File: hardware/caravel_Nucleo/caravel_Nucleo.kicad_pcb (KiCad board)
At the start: 2 copper layers, 68.1 x 92.5 mm, 91 parts, among them J1 USB_B_Micro - 10118193-0001LF, J10 Conn_01x11_Female, J11 Conn_01x02, J12 Conn_01x02_Male, J2 Conn_01x02_Female, J3 Conn_01x02_Male, J4 Conn_01x04_Female, J5 Conn_01x02_Male, J6 Conn_01x02_Male, J7 Conn_01x06_Female, J8 Conn_01x03, J9 Conn_01x03, SW1 SW_Push - SKQGADE010, T1 Logo, T2 Logo, U1 FT232H, U10 MCP4661, U11 TAR5SxxU_SOT353F, U12 NUCLEO144-F746ZG, U2 SN74LVC1G125DCKR, U3 SN74LVC1G125DCKR, U4 MCP1319MT-29LE-OT, U5 TAR5SxxU_SOT353F, U6 TAR5SxxU_SOT353F, U7 W25Q32FVSS, U8 caravel_breakout, U9 MIC2211-AAYML-TR, X1 DSC6001_10MHZ, Y1 CSTNE12M0GH5L000R0

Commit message: Move components to local library
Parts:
- C1, C10, C11, C12, C13, C14, C15, C16, C17, C18, C19, C2, C20, C21, C22, C23, C24, C3, C4, C5, C6, C7, C8, C9: footprint Capacitor_SMD:C_0805_2012Metric -> caravel_Nucleo-footprints:C_0805_2012Metric
- D1, D2, D3, D4: footprint LED_SMD:LED_1206_3216Metric -> caravel_Nucleo-footprints:LED_1206_3216Metric
- J1: footprint strive_foot_prints:FCI_10118193-0001LF -> caravel_Nucleo-footprints:FCI_10118193-0001LF
- J10: footprint Connector_PinHeader_2.54mm:PinHeader_1x11_P2.54mm_Vertical -> caravel_Nucleo-footprints:PinHeader_1x11_P2.54mm_Vertical
- J11, J12, J2, J3, J5, J6: footprint Connector_PinHeader_2.54mm:PinHeader_1x02_P2.54mm_Vertical -> caravel_Nucleo-footprints:PinHeader_1x02_P2.54mm_Vertical
- J4: footprint Connector_PinHeader_2.54mm:PinHeader_1x04_P2.54mm_Vertical -> caravel_Nucleo-footprints:PinHeader_1x04_P2.54mm_Vertical
- J7: footprint Connector_PinHeader_2.54mm:PinHeader_1x06_P2.54mm_Vertical -> caravel_Nucleo-footprints:PinHeader_1x06_P2.54mm_Vertical
- J8, J9: footprint Connector_PinHeader_2.54mm:PinHeader_1x03_P2.54mm_Vertical -> caravel_Nucleo-footprints:PinHeader_1x03_P2.54mm_Vertical
- R1, R10, R11, R12, R13, R14, R15, R16, R17, R18, R19, R2, R20, R21, R22, R23, R24, R25, R26, R27, R28, R29, R3, R30, R31, R32, R33, R4, R5, R6, R7, R8, R9: footprint Resistor_SMD:R_0805_2012Metric -> caravel_Nucleo-footprints:R_0805_2012Metric
- SW1: footprint strive_foot_prints:SW4-SMD-5.2X5.2X1.5MM -> caravel_Nucleo-footprints:SW4-SMD-5.2X5.2X1.5MM
- T1: footprint Caravel_Board:logo -> caravel_Nucleo-footprints:logo
- T2: footprint Caravel_Board:ef_logo -> caravel_Nucleo-footprints:ef_logo
- TP1: footprint TestPoint:TestPoint_Bridge_Pitch2.54mm_Drill1.0mm -> caravel_Nucleo-footprints:TestPoint_Bridge_Pitch2.54mm_Drill1.0mm
- U1: footprint Package_DFN_QFN:QFN-48-1EP_8x8mm_P0.5mm_EP6.2x6.2mm -> caravel_Nucleo-footprints:QFN-48-1EP_8x8mm_P0.5mm_EP6.2x6.2mm
- U10: footprint Caravel_Board:QFN-16-1EP_4x4mm_P0.65mm_EP2.5x2.5mm -> caravel_Nucleo-footprints:QFN-16-1EP_4x4mm_P0.65mm_EP2.5x2.5mm
- U11, U5, U6: footprint Caravel_Board:SOT-353F -> caravel_Nucleo-footprints:SOT-353F
- U12: footprint Caravel_Board:ST_Morpho_Connectors_144 -> caravel_Nucleo-footprints:ST_Morpho_Connectors_144
- U2, U3: footprint strive_foot_prints:SOT65P210X110-5N -> caravel_Nucleo-footprints:SOT65P210X110-5N
- U4: footprint Caravel_Board:PoR_5_SOT23 -> caravel_Nucleo-footprints:PoR_5_SOT23
- U7: footprint strive_foot_prints:SOIC127P790X216-8N -> caravel_Nucleo-footprints:SOIC127P790X216-8N
- U8: footprint Caravel_Board:caravel_breakout_flexy_rev3D -> caravel_Nucleo-footprints:caravel_breakout_flexy_rev3D
- U9: footprint Caravel_Board:10-pin_MLF_P0.5 -> caravel_Nucleo-footprints:10-pin_MLF_P0.5
- X1: footprint strive_foot_prints:DSC6001JE1A-010.0000 -> caravel_Nucleo-footprints:DSC6001JE1A-010.0000
- Y1: footprint strive_foot_prints:CSTNE12M0GH5L000R0 -> caravel_Nucleo-footprints:CSTNE12M0GH5L000R0

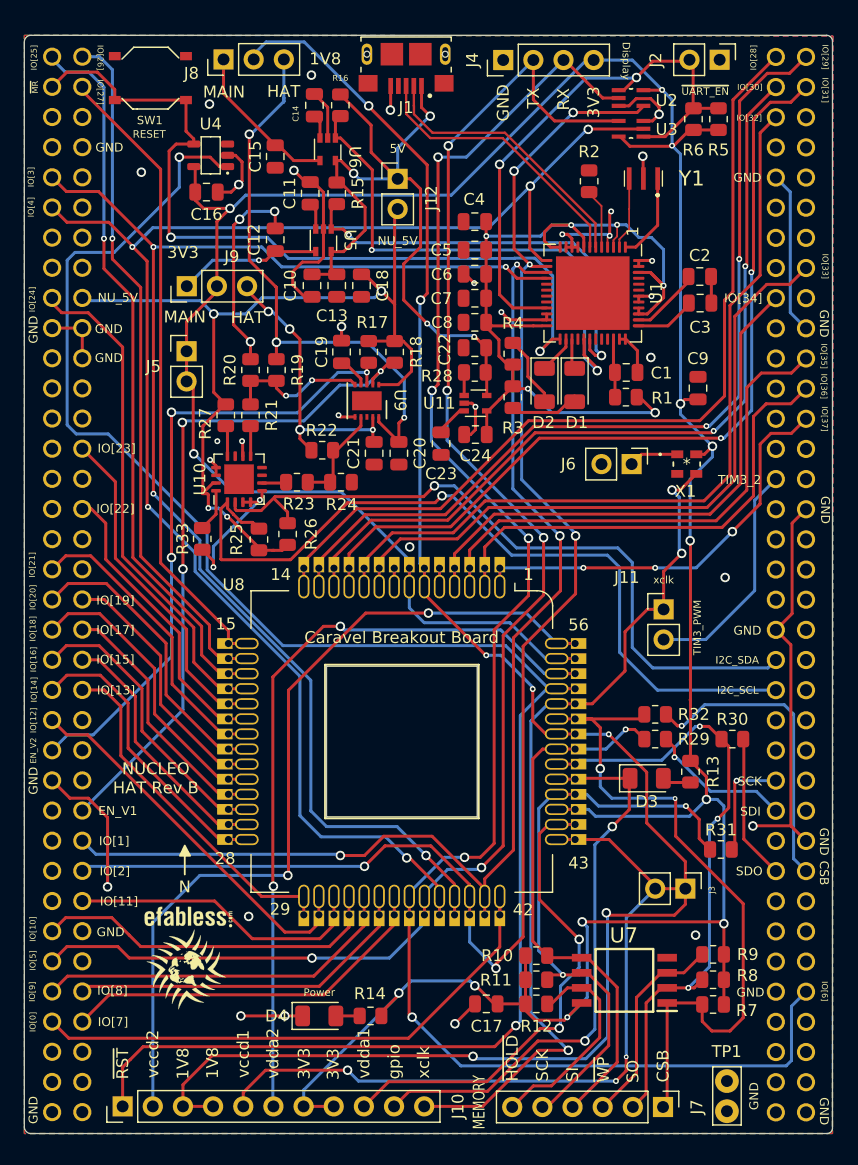
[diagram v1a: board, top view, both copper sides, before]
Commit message: Update PCB components
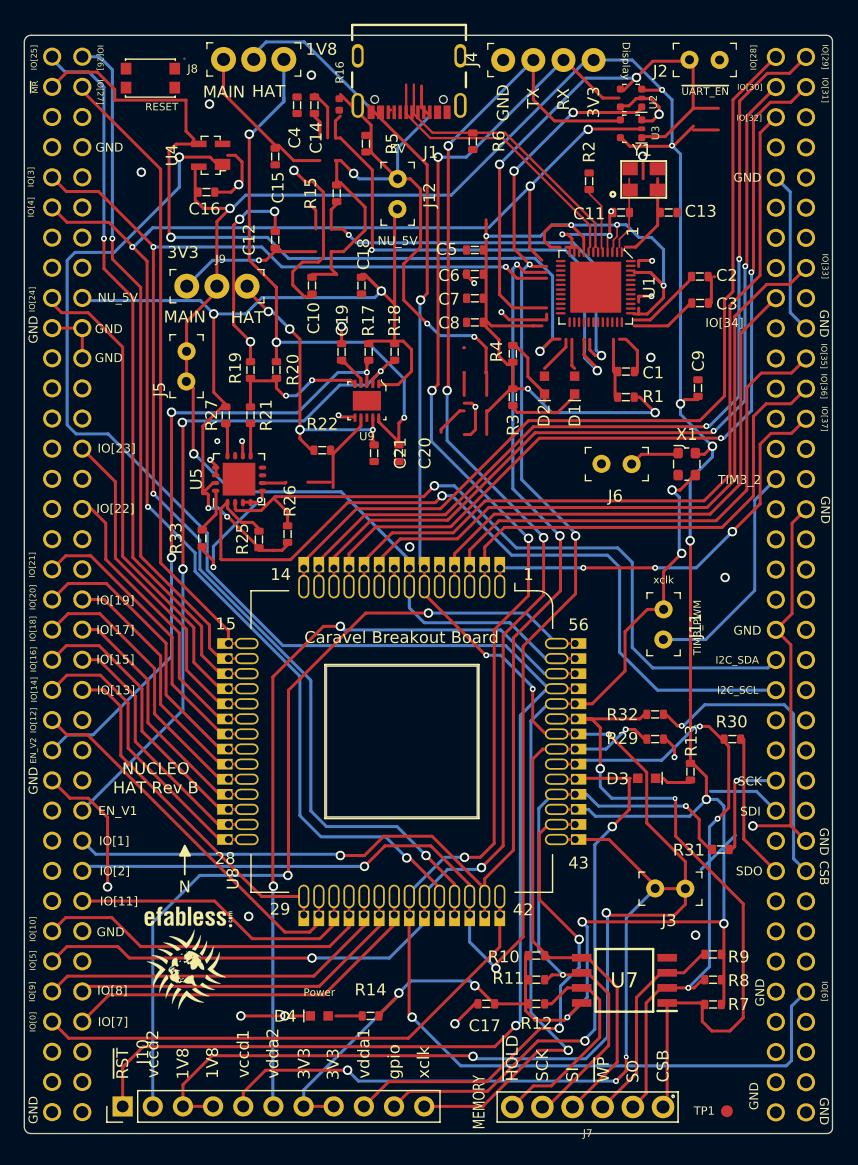
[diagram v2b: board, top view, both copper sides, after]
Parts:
- removed C22: 1uf - CC0805KKX5R8BB105, caravel_Nucleo-footprints:C_0805_2012Metric
- removed C23: 0.01uf - CC0805KRX7R9BB103, caravel_Nucleo-footprints:C_0805_2012Metric
- removed C24: 10uf - CC0805KKX5R8BB106, caravel_Nucleo-footprints:C_0805_2012Metric
- removed R23: 4.99K 1% - 0805W8F1202T5E, caravel_Nucleo-footprints:R_0805_2012Metric
- removed R24: 4.02K 1% - 0805W8F1202T5E, caravel_Nucleo-footprints:R_0805_2012Metric
- removed R28: 10k, caravel_Nucleo-footprints:R_0805_2012Metric
- removed U10: MCP4661, caravel_Nucleo-footprints:QFN-16-1EP_4x4mm_P0.65mm_EP2.5x2.5mm
- removed U11, U6: TAR5SxxU_SOT353F, caravel_Nucleo-footprints:SOT-353F
- C1: value 0.01uf - CC0805JRX7R9BB103 -> C_10n_0603; footprint caravel_Nucleo-footprints:C_0805_2012Metric -> antmicro-footprints:0603-cap
- C10: value 1uf - CC0805KKX5R8BB105 -> C_4u7_0603; footprint caravel_Nucleo-footprints:C_0805_2012Metric -> antmicro-footprints:0603-cap
- C11: value 0.01uf - CC0805KRX7R9BB103 -> C_18p_0603; footprint caravel_Nucleo-footprints:C_0805_2012Metric -> antmicro-footprints:0603-cap
- C12, C15: value 10uf - CC0805KKX5R8BB106 -> C_100n_0603; footprint caravel_Nucleo-footprints:C_0805_2012Metric -> antmicro-footprints:0603-cap
- C13: value 1uf - CC0805KKX5R8BB105 -> C_18p_0603; footprint caravel_Nucleo-footprints:C_0805_2012Metric -> antmicro-footprints:0603-cap
- C14: value 0.01uf - CC0805KRX7R9BB103 -> C_4u7_0603; footprint caravel_Nucleo-footprints:C_0805_2012Metric -> antmicro-footprints:0603-cap
- C16, C17, C2, C3, C4, C5, C6, C7, C8, C9: value 0.1uf - CC0805KRX7R9BB104 -> C_100n_0603; footprint caravel_Nucleo-footprints:C_0805_2012Metric -> antmicro-footprints:0603-cap
- C18, C20, C21: value 1uf - CC0805KKX5R8BB105 -> C_1u_0603; footprint caravel_Nucleo-footprints:C_0805_2012Metric -> antmicro-footprints:0603-cap
- C19: value 0.01uf - CC0805KRX7R9BB103 -> C_10n_0603; footprint caravel_Nucleo-footprints:C_0805_2012Metric -> antmicro-footprints:0603-cap
- D1, D2, D3, D4: value LED - 17-215SURC/S530-A2/TR8 -> KP-1608ZGC; footprint caravel_Nucleo-footprints:LED_1206_3216Metric -> antmicro-footprints:LED_0603
- J1: value USB_B_Micro - 10118193-0001LF -> USB4105-GF-A; footprint caravel_Nucleo-footprints:FCI_10118193-0001LF -> antmicro-footprints:GCT_USB4105-GF-A
- J10: value Conn_01x11_Female -> PinHeader_1x11; footprint caravel_Nucleo-footprints:PinHeader_1x11_P2.54mm_Vertical -> antmicro-footprints:PinHeader_1x11_P2.54_Vertical
- J11: value Conn_01x02 -> PinHeader_1x02; footprint caravel_Nucleo-footprints:PinHeader_1x02_P2.54mm_Vertical -> antmicro-footprints:PinHeader_1x2_P2.54mm
- J12, J3, J5, J6: value Conn_01x02_Male -> PinHeader_1x02; footprint caravel_Nucleo-footprints:PinHeader_1x02_P2.54mm_Vertical -> antmicro-footprints:PinHeader_1x2_P2.54mm
- J2: value Conn_01x02_Female -> M20-9990246; footprint caravel_Nucleo-footprints:PinHeader_1x02_P2.54mm_Vertical -> antmicro-footprints:PinHeader_1x2_P2.54mm
- J4: value Conn_01x04_Female -> 61300411121; footprint caravel_Nucleo-footprints:PinHeader_1x04_P2.54mm_Vertical -> antmicro-footprints:PinHeader_1x4_P2.54mm_Drill1.02mm
- J7: value Conn_01x06_Female -> 61300611121; footprint caravel_Nucleo-footprints:PinHeader_1x06_P2.54mm_Vertical -> antmicro-footprints:61300611121
- J8, J9: value Conn_01x03 -> 640456-3; footprint caravel_Nucleo-footprints:PinHeader_1x03_P2.54mm_Vertical -> antmicro-footprints:PinHeader_1x3_P2.54_Drill1.1mm
- R1, R10, R11, R12, R7, R8, R9: value 10k - RC0805FR-0710KL -> R_10k_0603; footprint caravel_Nucleo-footprints:R_0805_2012Metric -> antmicro-footprints:0603-res
- R13, R14: value 82 - 0805W8F820JT5E -> R_470R_0603; footprint caravel_Nucleo-footprints:R_0805_2012Metric -> antmicro-footprints:0603-res
- R15: value 10k -> R_15k_0603; footprint caravel_Nucleo-footprints:R_0805_2012Metric -> antmicro-footprints:0603-res
- R16: value 10k -> R_34k_0402; footprint caravel_Nucleo-footprints:R_0805_2012Metric -> antmicro-footprints:0402-res
- R17, R18, R27: value 10k -> R_10k_0603; footprint caravel_Nucleo-footprints:R_0805_2012Metric -> antmicro-footprints:0603-res
- R19: value 360 1% - 0805W8F1202T5E -> R_68k_0603; footprint caravel_Nucleo-footprints:R_0805_2012Metric -> antmicro-footprints:0603-res
- R2: value 12K 1% - 0805W8F1202T5E -> R_12k_0603; footprint caravel_Nucleo-footprints:R_0805_2012Metric -> antmicro-footprints:0603-res
- R20: value 4.99K 1% - 0805W8F1202T5E -> R_41k2_0603; footprint caravel_Nucleo-footprints:R_0805_2012Metric -> antmicro-footprints:0603-res
- R21: value 499 1% - 0805W8F1202T5E -> R_10k_0603; footprint caravel_Nucleo-footprints:R_0805_2012Metric -> antmicro-footprints:0603-res
- R22: value 4.22K 1% - 0805W8F1202T5E -> R_10k_0603; footprint caravel_Nucleo-footprints:R_0805_2012Metric -> antmicro-footprints:0603-res
- R25, R26: value 4.7K 1% - 0805W8F1202T5E -> R_4k7_0603; footprint caravel_Nucleo-footprints:R_0805_2012Metric -> antmicro-footprints:0603-res
- R29, R30, R31, R32, R33: value 0 -> R_0R_0603; footprint caravel_Nucleo-footprints:R_0805_2012Metric -> antmicro-footprints:0603-res
- R3, R4: value 150 - 0805W8J0151T5E -> R_470R_0603; footprint caravel_Nucleo-footprints:R_0805_2012Metric -> antmicro-footprints:0603-res
- R5, R6: value 10k -> R_5k1_0603; footprint caravel_Nucleo-footprints:R_0805_2012Metric -> antmicro-footprints:0603-res
- SW1: value SW_Push - SKQGADE010 -> KMR2; footprint caravel_Nucleo-footprints:SW4-SMD-5.2X5.2X1.5MM -> antmicro-footprints:SW_SPST_4.2x2.8
- T1: footprint caravel_Nucleo-footprints:logo -> antmicro-footprints:efabless_logo_2
- T2: footprint caravel_Nucleo-footprints:ef_logo -> antmicro-footprints:efabless_logo
- TP1: value TestPoint -> TP_SMD1MM; footprint caravel_Nucleo-footprints:TestPoint_Bridge_Pitch2.54mm_Drill1.0mm -> antmicro-footprints:Testpoint_smd_1mm
- U1: value FT232H -> FT232HQ; footprint caravel_Nucleo-footprints:QFN-48-1EP_8x8mm_P0.5mm_EP6.2x6.2mm -> antmicro-footprints:QFN-48-1EP_6x6mm
- U12: value NUCLEO144-F746ZG -> NUCLEO144-F429ZI; footprint caravel_Nucleo-footprints:ST_Morpho_Connectors_144 -> antmicro-footprints:ST_Morpho_Connectors_144
- U2, U3: footprint caravel_Nucleo-footprints:SOT65P210X110-5N -> antmicro-footprints:SOT-353
- U4: value MCP1319MT-29LE-OT -> MAX811REUS+T; footprint caravel_Nucleo-footprints:PoR_5_SOT23 -> antmicro-footprints:SOT-143-4
- U5: value TAR5SxxU_SOT353F -> MCP4661-103E/ML; footprint caravel_Nucleo-footprints:SOT-353F -> antmicro-footprints:QFN-16_EP_4x4_Pitch0.65mm
- U7: footprint caravel_Nucleo-footprints:SOIC127P790X216-8N -> antmicro-footprints:SOIC127P790X216-8N
- U8: footprint caravel_Nucleo-footprints:caravel_breakout_flexy_rev3D -> antmicro-footprints:caravel_breakout
- U9: footprint caravel_Nucleo-footprints:10-pin_MLF_P0.5 -> antmicro-footprints:DFN-10-1EP_3x3mm
- X1: value DSC6001_10MHZ -> ECS-2520MVLC-100-BN-TR; footprint caravel_Nucleo-footprints:DSC6001JE1A-010.0000 -> antmicro-footprints:Oscillator_SMD_ECS_2520MV-xxx-xx-4Pin_2.5x2.0mm
- Y1: value CSTNE12M0GH5L000R0 -> ABM8G-12.000MHZ-18-D2Y-T; footprint caravel_Nucleo-footprints:CSTNE12M0GH5L000R0 -> antmicro-footprints:KX-7
- moved R5 29.8 mm to (128.8, 26.5), turned to -90 degrees
- moved C13 28.6 mm to (154.3, 32.3), turned to 0 degrees
- moved C11 26.2 mm to (150.3, 32.3), turned to 180 degrees
- moved U5 21.3 mm to (118.1, 54.8), turned to 90 degrees
- moved R6 18.7 mm to (137.8, 26.3), turned to -90 degrees
- moved C4 17.9 mm to (123.0, 23.3), turned to 90 degrees
- moved J7 6.35 mm to (147.5, 107.6), turned to 180 degrees
- moved TP1 2.54 mm to (159.2, 108.0), turned to 0 degrees
- moved U1 0.56 mm to (148.2, 38.6)
- moved J1 0.28 mm to (132.4, 19.1)
- moved R16 0.12 mm to (126.5, 23.2), turned to -90 degrees
- moved C1 0.07 mm to (150.7, 45.7), turned to 0 degrees
- turned J2 to 180 degrees
- turned J12 to -90 degrees
- turned J3 to 180 degrees
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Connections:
- net EN_VOUT1 renamed /EN_VOUT1
- net EN_VOUT2 renamed /EN_VOUT2
- net Net-(C2-Pad2) renamed /VCORE
- net Net-(C3-Pad2) renamed /VCCA
- net Net-(R2-Pad2) renamed /REF
- net SPI5_CS renamed /SPI5_CS
- net SPI5_MISO renamed /SPI5_MISO
- net SPI5_MOSI renamed /SPI5_MOSI
- net SPI5_SCK renamed /SPI5_SCK
- net TIM3_CH2 renamed /TIM3_CH2
- net UART8_RX renamed /UART8_RX
- net UART8_TX renamed /UART8_TX
- net mprj_io[0] renamed /mprj_io[0]
- net mprj_io[10] renamed /mprj_io[10]
- net mprj_io[11] renamed /mprj_io[11]
- net mprj_io[12] renamed /mprj_io[12]
- net mprj_io[13] renamed /mprj_io[13]
- net mprj_io[14] renamed /mprj_io[14]
- net mprj_io[15] renamed /mprj_io[15]
- net mprj_io[16] renamed /mprj_io[16]
- net mprj_io[17] renamed /mprj_io[17]
- net mprj_io[18] renamed /mprj_io[18]
- net mprj_io[19] renamed /mprj_io[19]
- net mprj_io[20] renamed /mprj_io[20]
- net mprj_io[21] renamed /mprj_io[21]
- net mprj_io[22] renamed /mprj_io[22]
- net mprj_io[23] renamed /mprj_io[23]
- net mprj_io[24] renamed /mprj_io[24]
- net mprj_io[25] renamed /mprj_io[25]
- net mprj_io[26] renamed /mprj_io[26]
- net mprj_io[27] renamed /mprj_io[27]
- net mprj_io[28] renamed /mprj_io[28]
- net mprj_io[29] renamed /mprj_io[29]
- net mprj_io[30] renamed /mprj_io[30]
- net mprj_io[31] renamed /mprj_io[31]
- net mprj_io[32] renamed /mprj_io[32]
- net mprj_io[33] renamed /mprj_io[33]
- net mprj_io[34] renamed /mprj_io[34]
- net mprj_io[35] renamed /mprj_io[35]
- net mprj_io[36] renamed /mprj_io[36]
- net mprj_io[37] renamed /mprj_io[37]
- net mprj_io[7] renamed /mprj_io[7]
- net mprj_io[8] renamed /mprj_io[8]
- net mprj_io[9] renamed /mprj_io[9]
- net vccd2 renamed /vccd2
- net vdda1 renamed /vdda1
- net vdda2 renamed /vdda2
- C1 pad 1: GND -> /FTDI_RESET
- C1 pad 2: Net-(C1-Pad2) -> AGND
- C10 pad 1: GND -> VBUS
- C10 pad 2: +5V -> AGND
- C11 pad 1: Net-(C11-Pad1) -> /XIN
- C11 pad 2: GND -> AGND
- C12 pad 1: GND -> AGND
- C12 pad 2: V3.3 -> VBUS
- C13 pad 1: GND -> /XOUT
- C13 pad 2: +5V -> AGND
- C14 pad 1: Net-(C14-Pad1) -> /FTDI_3V3
- C14 pad 2: GND -> AGND
- C15 pad 1: GND -> AGND
- C15 pad 2: V1.8 -> /FTDI_3V3
- C16 pad 1: GND -> +3V3
- C16 pad 2: vdda -> AGND
- C17 pad 1: vdda -> +3V3
- C17 pad 2: GND -> AGND
- C18 pad 1: GND -> /NU_5V
- C18 pad 2: NU_5V -> AGND
- C19 pad 1: Net-(C19-Pad1) -> AGND
- C19 pad 2: GND -> Net-(C19-Pad2)
- C2 pad 1: GND -> AGND
- C20 pad 1: VOUT1 -> +3V3
- C20 pad 2: GND -> AGND
- C21 pad 1: VOUT2 -> +1V8
- C21 pad 2: GND -> AGND
- C3 pad 1: GND -> AGND
- C4 pad 1: GND -> /FTDI_3V3
- C4 pad 2: FTDI_V3.3 -> AGND
- C5 pad 1: GND -> /FTDI_3V3
- C5 pad 2: FTDI_V3.3 -> AGND
- C6 pad 1: GND -> /FTDI_3V3
- C6 pad 2: FTDI_V3.3 -> AGND
- C7 pad 1: GND -> /FTDI_3V3
- C7 pad 2: FTDI_V3.3 -> AGND
- C8 pad 1: GND -> /FTDI_3V3
- C8 pad 2: FTDI_V3.3 -> AGND
- C9 pad 1: GND -> AGND
- C9 pad 2: vdda -> +3V3
- D1 pad 1: Net-(D1-Pad1) -> /FTDI_3V3
- D2 pad 1: Net-(D2-Pad1) -> /FTDI_3V3
- D3 pad 1: gpio -> Net-(D3-Pad1)
- D3 pad 2: Net-(D3-Pad2) -> /gpio
- D4 pad 1: GND -> Net-(D4-Pad1)
- D4 pad 2: Net-(D4-Pad2) -> AGND
- J10 pad 10: gpio -> /gpio
- J10 pad 3: vccd -> +1V8
- J10 pad 4: vccd -> +1V8
- J10 pad 5: vccd -> +1V8
- J10 pad 7: vdda -> +3V3
- J10 pad 8: vdda -> +3V3
- J12 pad 2: NU_5V -> /NU_5V
- J2 pad 1: GND -> AGND
- J2 pad 2: ~{UART_EN} -> /~{UART_EN}
- J3 pad 1: vccd -> +1V8
- J3 pad 2: vccd -> +1V8
- J4 pad 1: GND -> AGND
- J4 pad 4: vdda -> +3V3
- J5 pad 1: vdda -> +3V3
- J5 pad 2: vdda -> +3V3
- J6 pad 2: GND -> AGND
- J7 pad 1: Caravel_CSB -> /Caravel_CSB
- J7 pad 2: Caravel_D1 -> /Caravel_D1
- J7 pad 3: ~{MEM_WP} -> /~{MEM_WP}
- J7 pad 4: Caravel_D0 -> /Caravel_D0
- J7 pad 5: Caravel_SCK -> /Caravel_SCK
- J7 pad 6: ~{MEM_HOLD} -> /~{MEM_HOLD}
- J8 pad 1: V1.8 -> /P0B
- J8 pad 2: vccd -> /P0A
- J8 pad 3: VOUT1 -> unconnected-(J8-Pad3)
- J9 pad 1: V3.3 -> /P1B
- J9 pad 2: vdda -> /P1A
- J9 pad 3: VOUT2 -> /LV_BOOSTER
- R1 pad 1: Net-(C1-Pad2) -> /FTDI_3V3
- R1 pad 2: FTDI_V3.3 -> /FTDI_RESET
- R10 pad 1: Caravel_D0 -> +3V3
- R10 pad 2: vdda -> /Caravel_D0
- R11 pad 1: Caravel_SCK -> +3V3
- R11 pad 2: vdda -> /Caravel_SCK
- R12 pad 1: ~{MEM_HOLD} -> +3V3
- R12 pad 2: vdda -> /~{MEM_HOLD}
- R13 pad 1: vdda -> Net-(D3-Pad1)
- R13 pad 2: Net-(D3-Pad2) -> +3V3
- R14 pad 1: vdda -> Net-(D4-Pad1)
- R14 pad 2: Net-(D4-Pad2) -> +3V3
- R15 pad 1: EN_V3.3 -> /P1A
- R15 pad 2: +5V -> +1V8
- R16 pad 1: EN_V1.8 -> AGND
- R16 pad 2: +5V -> /P1B
- R17 pad 2: NU_5V -> /NU_5V
- R18 pad 2: NU_5V -> /NU_5V
- R19 pad 1: Net-(R19-Pad1) -> /P0A
- R19 pad 2: VOUT1 -> +3V3
- R2 pad 1: GND -> AGND
- R20 pad 1: GND -> AGND
- R20 pad 2: Net-(R19-Pad1) -> /P0B
- R21 pad 1: Net-(R21-Pad1) -> /LV_BOOSTER
- R21 pad 2: Net-(R19-Pad1) -> +1V8
- R22 pad 1: Net-(R22-Pad1) -> /~{UART_EN}
- R22 pad 2: VOUT2 -> +3V3
- R25 pad 1: NU_5V -> /I2C4_SCL
- R25 pad 2: I2C4_SCL -> /NU_5V
- R26 pad 1: NU_5V -> /I2C4_SDA
- R26 pad 2: I2C4_SDA -> /NU_5V
- R27 pad 1: Net-(R27-Pad1) -> /NU_5V
- R27 pad 2: NU_5V -> Net-(R27-Pad2)
- R29 pad 1: Caravel_D0 -> /SPI4_MOSI
- R29 pad 2: SPI4_MOSI -> /Caravel_D0
- R3 pad 1: Net-(D1-Pad2) -> /~{TX_LED}
- R3 pad 2: FTDI_V3.3 -> Net-(D1-Pad2)
- R30 pad 1: Caravel_D1 -> /SPI4_MISO
- R30 pad 2: SPI4_MISO -> /Caravel_D1
- R31 pad 1: Caravel_SCK -> /SPI4_SCK
- R31 pad 2: SPI4_SCK -> /Caravel_SCK
- R32 pad 1: Caravel_CSB -> /SPI4_CS
- R32 pad 2: SPI4_CS -> /Caravel_CSB
- R33 pad 1: GND -> AGND
- R4 pad 1: Net-(D2-Pad2) -> /~{RX_LED}
- R4 pad 2: FTDI_V3.3 -> Net-(D2-Pad2)
- R5 pad 1: vdda -> /CC2
- R5 pad 2: ~{UART_EN} -> AGND
- R6 pad 1: vdda -> /CC1
- R6 pad 2: ~{UART_EN} -> AGND
- R7 pad 1: Caravel_CSB -> +3V3
- R7 pad 2: vdda -> /Caravel_CSB
- R8 pad 1: Caravel_D1 -> +3V3
- R8 pad 2: vdda -> /Caravel_D1
- R9 pad 1: ~{MEM_WP} -> +3V3
- R9 pad 2: vdda -> /~{MEM_WP}
- SW1 pad 1: ~{MR} -> AGND
- SW1 pad 2: GND -> /~{MR}
- TP1 pad 1: GND -> AGND
- U1 pad 1: Net-(U1-Pad1) -> /XIN
- U1 pad 10: GND -> AGND
- U1 pad 11: GND -> AGND
- U1 pad 12: FTDI_V3.3 -> /FTDI_3V3
- U1 pad 2: Net-(U1-Pad2) -> /XOUT
- U1 pad 21: ~{UART_EN} -> /~{UART_EN}
- U1 pad 22: GND -> AGND
- U1 pad 23: GND -> AGND
- U1 pad 24: FTDI_V3.3 -> /FTDI_3V3
- U1 pad 25: ~{MR} -> /~{MR}
- U1 pad 26: Net-(D2-Pad1) -> /~{RX_LED}
- U1 pad 27: Net-(D1-Pad1) -> /~{TX_LED}
- U1 pad 29: EN_V1.8 -> /EN_1V8
- U1 pad 3: FTDI_V3.3 -> /FTDI_3V3
- U1 pad 30: EN_V3.3 -> /EN_3V3
- U1 pad 34: Net-(C1-Pad2) -> /FTDI_RESET
- U1 pad 35: GND -> AGND
- U1 pad 36: GND -> AGND
- U1 pad 39: FTDI_V3.3 -> /FTDI_3V3
- U1 pad 4: GND -> AGND
- U1 pad 40: FTDI_V3.3 -> VBUS
- U1 pad 41: GND -> AGND
- U1 pad 42: GND -> AGND
- U1 pad 46: FTDI_V3.3 -> /FTDI_3V3
- U1 pad 47: GND -> AGND
- U1 pad 48: GND -> AGND
- U1 pad 49: (no net) -> AGND
- U1 pad 6: FTDI_D- -> /FTDI_DN
- U1 pad 7: FTDI_D+ -> /FTDI_DP
- U1 pad 8: FTDI_V3.3 -> /FTDI_3V3
- U1 pad 9: GND -> AGND
- U12 pad 104: GND -> AGND
- U12 pad 111: GND -> AGND
- U12 pad 113: I2C4_SDA -> /I2C4_SDA
- U12 pad 115: I2C4_SCL -> /I2C4_SCL
- U12 pad 121: SPI4_SCK -> /SPI4_SCK
- U12 pad 123: SPI4_MOSI -> /SPI4_MOSI
- U12 pad 126: GND -> AGND
- U12 pad 127: SPI4_MISO -> /SPI4_MISO
- U12 pad 128: SPI4_CS -> /SPI4_CS
- U12 pad 135: GND -> AGND
- U12 pad 143: GND -> AGND
- U12 pad 144: GND -> AGND
- U12 pad 18: NU_5V -> /NU_5V
- U12 pad 19: GND -> AGND
- U12 pad 20: GND -> AGND
- U12 pad 22: GND -> AGND
- U12 pad 3: ~{MR} -> /~{MR}
- U12 pad 49: GND -> AGND
- U12 pad 60: GND -> AGND
- U12 pad 71: GND -> AGND
- U12 pad 72: GND -> AGND
- U12 pad 8: GND -> AGND
- U12 pad 81: GND -> AGND
- U12 pad 92: GND -> AGND
- U2 pad 1: ~{UART_EN} -> /~{UART_EN}
- U2 pad 3: GND -> AGND
- U2 pad 5: vdda -> /FTDI_3V3
- U3 pad 1: ~{UART_EN} -> /~{UART_EN}
- U3 pad 3: GND -> AGND
- U3 pad 5: vdda -> +3V3
- U4 pad 1: ~{RST} -> AGND
- U4 pad 2: GND -> ~{RST}
- U4 pad 3: unconnected-(U4-Pad3) -> /~{MR}
- U4 pad 4: ~{MR} -> +3V3
- U5 pad 1: EN_V3.3 -> /I2C4_SCL
- U5 pad 2: GND -> /I2C4_SDA
- U5 pad 3: Net-(C11-Pad1) -> AGND
- U5 pad 4: V3.3 -> AGND
- U5 pad 5: +5V -> /P1B
- U7 pad 1: Caravel_CSB -> /Caravel_CSB
- U7 pad 2: Caravel_D1 -> /Caravel_D1
- U7 pad 3: ~{MEM_WP} -> /~{MEM_WP}
- U7 pad 4: GND -> AGND
- U7 pad 5: Caravel_D0 -> /Caravel_D0
- U7 pad 6: Caravel_SCK -> /Caravel_SCK
- U7 pad 7: ~{MEM_HOLD} -> /~{MEM_HOLD}
- U7 pad 8: vdda -> +3V3
- U8 pad 43: vccd -> +1V8
- U8 pad 45: vdda -> +3V3
- U8 pad 46: Caravel_SCK -> /Caravel_SCK
- U8 pad 47: gpio -> /gpio
- U8 pad 48: Caravel_D1 -> /Caravel_D1
- U8 pad 49: Caravel_D0 -> /Caravel_D0
- U8 pad 5: GND -> AGND
- U8 pad 50: vccd -> +1V8
- U8 pad 51: Caravel_CSB -> /Caravel_CSB
- U8 pad 55: vdda -> +3V3
- U8 pad 6: vccd -> +1V8
- U8 pad 7: vdda -> +3V3
- U8 pad 8: GND -> AGND
- U9 pad 1: NU_5V -> /NU_5V
- U9 pad 10: VOUT1 -> +3V3
- U9 pad 4: Net-(C19-Pad1) -> Net-(C19-Pad2)
- U9 pad 5: Net-(R19-Pad1) -> /P0W
- U9 pad 6: GND -> AGND
- U9 pad 7: Net-(R22-Pad1) -> /P1W
- U9 pad 9: VOUT2 -> +1V8
- X1 pad 2: GND -> AGND
- X1 pad 4: vdda -> +3V3
- Y1 pad 1: Net-(U1-Pad1) -> /XIN
- Y1 pad 2: GND -> AGND
- Y1 pad 3: Net-(U1-Pad2) -> /XOUT
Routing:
- net +3V3: track 0.00 -> 390.7 mm, vias 0 -> 20
- net vdda: track 283.0 -> 0.00 mm, vias 13 -> 0
- net +1V8: track 0.00 -> 248.0 mm, vias 0 -> 16
- net vccd: track 218.9 -> 0.00 mm, vias 10 -> 0
- net AGND: track 0.00 -> 217.7 mm, vias 0 -> 25
- net GND: track 172.0 -> 0.00 mm, vias 36 -> 0
- net /FTDI_3V3: track 0.00 -> 92.7 mm, vias 0 -> 6
- net NU_5V: track 80.7 -> 0.00 mm, vias 4 -> 0
- net /NU_5V: track 0.00 -> 80.7 mm, vias 0 -> 4
- net (no net): track 0.00 -> 77.5 mm, vias 0 -> 10
- net FTDI_V3.3: track 77.4 -> 0.00 mm, vias 6 -> 0
- net ~{MR}: track 69.3 -> 0.00 mm, vias 2 -> 0
- net /~{MR}: track 0.00 -> 69.3 mm, vias 0 -> 2
- net I2C4_SCL: track 68.9 -> 0.00 mm, vias 1 -> 0
- net /I2C4_SCL: track 0.00 -> 68.9 mm, vias 0 -> 1
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- removed copper zone on B.Cu, net GND
- removed copper zone on F.Cu, net GND

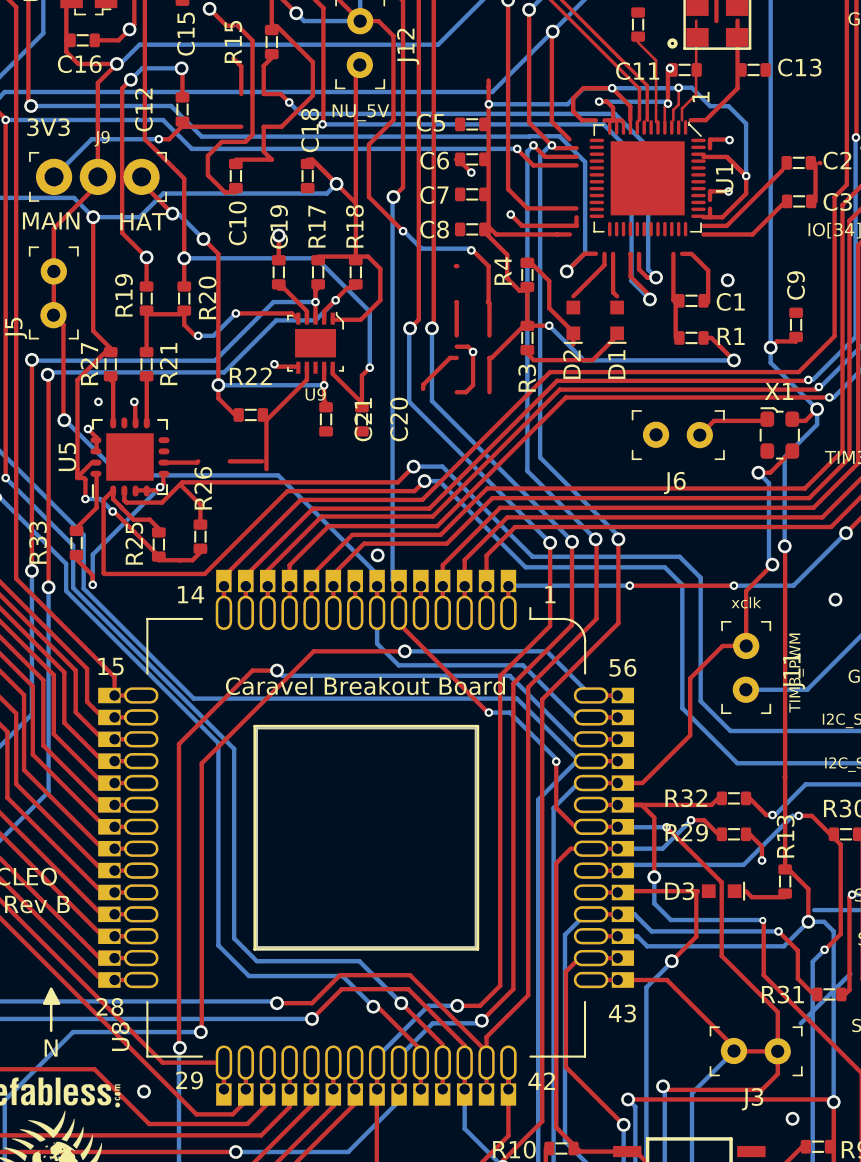
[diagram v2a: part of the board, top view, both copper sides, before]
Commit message: Update FTDI footprint on PCB
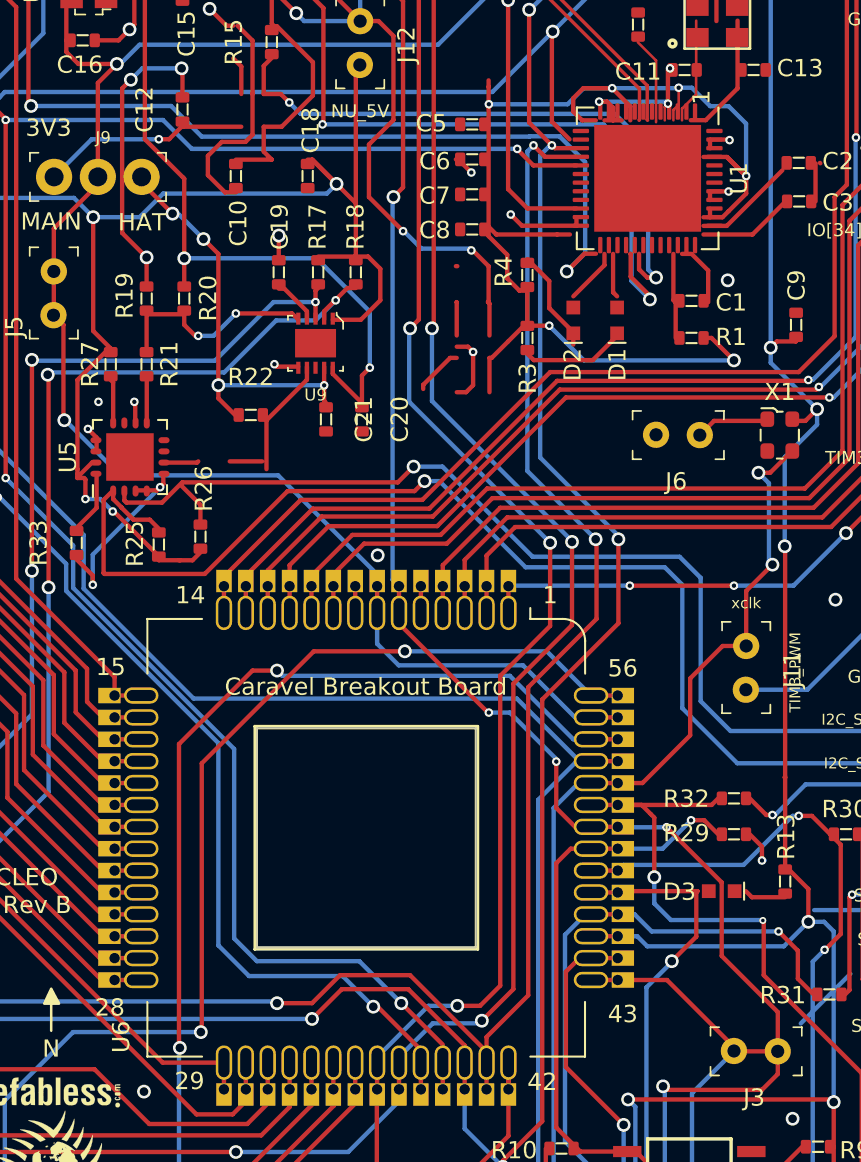
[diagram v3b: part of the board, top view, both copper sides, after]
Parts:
- removed U8: caravel_breakout, antmicro-footprints:caravel_breakout
- added U6: Caravel_breakout_PCB, antmicro-footprints:caravel_breakout, F.Cu at (131.8, 76.9)
- U1: footprint antmicro-footprints:QFN-48-1EP_6x6mm -> antmicro-footprints:QFN-48-1EP_8x8mm_P0.5mm_EP6.2x6.2mm_FT232HQ_marking
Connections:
- net ~{RST} renamed /~{RST}
- C18 pad 1: /NU_5V -> Net-(C18-Pad1)
- D3 pad 2: /gpio -> AGND
- J1 pad A6: /USB_DP -> /FTDI_DP
- J1 pad A7: /USB_DN -> /FTDI_DN
- J1 pad B6: /USB_DP -> /FTDI_DP
- J1 pad B7: /USB_DN -> /FTDI_DN
- R13 pad 2: +3V3 -> Net-(R13-Pad2)
- R17 pad 2: /NU_5V -> Net-(C18-Pad1)
- R18 pad 2: /NU_5V -> Net-(C18-Pad1)
- R25 pad 2: /NU_5V -> Net-(C18-Pad1)
- R26 pad 2: /NU_5V -> Net-(C18-Pad1)
- R27 pad 1: /NU_5V -> Net-(C18-Pad1)
- U1 pad 12: /FTDI_3V3 -> (no net)
- U1 pad 24: /FTDI_3V3 -> (no net)
- U1 pad 3: /FTDI_3V3 -> (no net)
- U1 pad 46: /FTDI_3V3 -> (no net)
- U1 pad 8: /FTDI_3V3 -> (no net)
- U5 pad 15: /NU_5V -> Net-(C18-Pad1)
- U9 pad 1: /NU_5V -> Net-(C18-Pad1)
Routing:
- net ~{RST}: track 0.00 -> 154.8 mm, vias 0 -> 2
- net /~{RST}: track 154.8 -> 0.00 mm, vias 2 -> 0
- net Net-(C18-Pad1): track 0.00 -> 83.3 mm, vias 0 -> 4
- net /NU_5V: track 80.7 -> 0.00 mm, vias 4 -> 0
- net /USB_DN: track 47.3 -> 0.00 mm
- net /FTDI_DN: track 0.00 -> 47.3 mm
- net /P1W: track 10.9 -> 2.06 mm
- net +3V3: track 390.7 -> 399.5 mm
- net AGND: track 217.7 -> 226.1 mm, vias 25 -> 27
- net (no net): track 77.5 -> 69.6 mm, vias 10 -> 7
- net Net-(D1-Pad2): track 5.95 -> 0.00 mm
- net /~{TX_LED}: track 0.00 -> 5.95 mm
- net Net-(R27-Pad2): track 2.59 -> 0.00 mm
- net /P0W: track 2.54 -> 0.00 mm
- net /LV_BOOSTER: track 0.00 -> 2.54 mm
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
